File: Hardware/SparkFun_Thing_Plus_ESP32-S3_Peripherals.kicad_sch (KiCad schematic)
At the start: 27 parts, among them J2 microSD_Friction, J3 JST_2mm_LiPo, J5 Qwiic_Vertical, U1 AP2112K-3.3, U7 MCP73831, U8 MAX17048

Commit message: Update rev number
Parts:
- renumbered C15 to C12, C14 to C2, C5 to C3, C18 to C4, C19 to C5, C16 to C8, C12 to C9, JP3 to JP1, U8 to U4, U7 to U5
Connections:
- net ESP33/SDIO3: now also R6.2; no longer R1.2
- net ESP34/SDIO_CMD: now also R1.2; no longer R6.2
- net ESP38/SDIO_CLK: now also R2.2; no longer R5.2
- net ESP39/SDIO0: now also R3.2; no longer R4.2
- net ESP40/SDIO1: now also R4.2; no longer R3.2
- net ESP47/SDIO2: now also R5.2; no longer R2.2
- net GND: now also U4.9 (GND)
- net +3.3V renamed 3.3V
- net +5V renamed 5V
- new net: J3.NC1, J3.NC2
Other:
- note added: "7-bit I2C Address: 0x36"

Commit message: Updates post review
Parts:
- added LP1: ~, SparkFun-Jumper:SMT-JUMPER_3_1-NC_TRACE_SILK, symbol SparkFun-Jumper:SolderJumper_3_Bridged12
- added Q1: DMG2305UX, SparkFun-Semiconductor-Standard:SOT23-3, symbol SparkFun-DiscreteSemi:Q_PMOS_4.2A_20V
- added R17, R18: 100k, SparkFun-Resistor:R_0402_1005Metric, symbol SparkFun-Resistor:100k_0402
- C3: value 1.0uF -> 10uF; footprint SparkFun-Capacitor:C_0402_1005Metric -> SparkFun-Capacitor:C_0603_1608Metric; symbol SparkFun-Capacitor:1.0uF_0402_16V_10% -> SparkFun-Capacitor:10uF_0603_6.3V_20%; PROD_ID CAP-14969 -> CAP-11015; Tolerance 10% -> 20%; Voltage 16V -> 6.3V
- U1: value AP2112K-3.3 -> RT9080-3.3; symbol SparkFun-Regulator:AP2112K-3.3 -> SparkFun-Regulator:RT9080-3.3; Imax (none) -> 600mA; Iq (none) -> 4µA; PROD_ID VREG-12457 -> VREG-19034; VMax (none) -> 6V
- renumbered JP1 to CHG1
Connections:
- net 3.3V: now also Q1.2 (S), R18.1; no longer C4.1, C5.1, C8.1, D6.1 (VDD), J2.4 (VDD), R1.1, R2.1, R3.1, R4.1, R5.1, R6.1
- net ESP45/Q_EN: now also R17.2
- net GND: now also LP1.1 (A), R17.1
- net ESP35/~{ALRT}: now reaches U4.5 (~{ALRT})
- net 5V renamed VIN
- new net: LP1.2 (C), Q1.1 (G), R18.2
- new net 3.3V_P: C4.1, C5.1, C8.1, D6.1 (VDD), J2.4 (VDD), Q1.3 (D), R1.1, R2.1, R3.1, R4.1, R5.1, R6.1
- new net ESP41/LP_CTL: LP1.3 (B)
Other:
- note added: "Move LP jumper to 41 side to enable low power control"
- note added: "Peripheral Power Control"
- moved on the sheet: C3, U1

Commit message: Add default on to Qwiic power.
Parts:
- added R19: 100k, SparkFun-Resistor:R_0402_1005Metric, symbol SparkFun-Resistor:100k_0402
- JP2: renamed from LP1; value ~ -> LP_CTL
- R17: value 100k -> 10k; symbol SparkFun-Resistor:100k_0402 -> SparkFun-Resistor:10k_0402; PROD_ID RES-13495 -> RES-14241
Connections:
- net 3.3V_P: now also R17.1
- net ESP45/Q_EN: now also R19.1
- net GND: now also R19.2; no longer R17.1
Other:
- note added: "Default: 3.3V_P is on, Q_EN is pulled up If LP_CTL jumper is cut, 3.3V_P is off, and Q_EN is pulled down"
- note added: "Move LP jumper to LP_CTL side to enable low power control"
- note removed: "Move LP jumper to 41 side to enable low power control"
- moved on the sheet: C3, J5, R17, R3, R4, U1

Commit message: Revise layout post design review
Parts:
- removed JP2: LP_CTL, SparkFun-Jumper:SMT-JUMPER_3_1-NC_TRACE_SILK, symbol SparkFun-Jumper:SolderJumper_3_Bridged12
- removed Q1: DMG2305UX, SparkFun-Semiconductor-Standard:SOT23-3, symbol SparkFun-DiscreteSemi:Q_PMOS_4.2A_20V
- removed R18: 100k, SparkFun-Resistor:R_0402_1005Metric, symbol SparkFun-Resistor:100k_0402
- added C14: 2.2uF, SparkFun-Capacitor:C_0402_1005Metric, symbol SparkFun-Capacitor:2.2uF_0402_10V_10%
- added JP2: LP_CTL, SparkFun-Jumper:SMT-JUMPER_2_NC_TRACE_SILK, symbol SparkFun-Jumper:SolderJumper_2_Bridged
- C3: footprint SparkFun-Capacitor:C_0603_1608Metric -> SparkFun-Capacitor:C_0402_1005Metric; symbol SparkFun-Capacitor:10uF_0603_6.3V_20% -> SparkFun-Capacitor:10uF_0402_6.3V_20%; PROD_ID CAP-11015 -> CAP-14848
- JP3: renamed from CHG1; value ~ -> CHG
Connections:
- net Q3V3 is gone; now on net 3.3V_P: C3.1, J5.2 (Pin_2), R3.1, R4.1, U1.5 (VOUT)
- net 3.3V: now also JP2.2 (B)
- net 3.3V_P: now also D6.4 (VDD); no longer D6.1 (VDD), R17.1
- net ESP46/LED: now also D6.3 (DIN); no longer D6.4 (DIN)
- net GND: now also D6.2 (VSS), C14.2; no longer D6.3 (VSS)
- net VIN: now also C14.1
- net at TP1.1: now also D6.1 (DOUT); no longer D6.2 (DOUT)
- new net: JP2.1 (A), R17.1
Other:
- note added: "Default: Peripheral Power is on If LP_CTL jumper is cut and ESP32 goes to sleep, Peripheral Power is turned off."
- note removed: "Default: 3.3V_P is on, Q_EN is pulled up If LP_CTL jumper is cut, 3.3V_P is off, and Q_EN is pulled down"
- note removed: "Move LP jumper to LP_CTL side to enable low power control"
- note removed: "Qwiic"
- moved on the sheet: C3, C4, C5, J2, J5, R1, R17, R19, R2, R3, R4, R5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

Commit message: Fix 330 prod ID. Update parts to new naming conventions
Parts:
- C12: Tolerance 10% -> 20%
- J3: footprint SparkFun-Connector:JST-2-SMD -> SparkFun-Connector:JST_SMD_2.0mm-2
- J5: value Qwiic_Vertical -> Qwiic_RA; footprint SparkFun-Connector:JST04_1MM_RA -> SparkFun-Connector:JST_SMD_1.0mm-4_RA
- JP2: value LP_CTL -> ~; footprint SparkFun-Jumper:SMT-JUMPER_2_NC_TRACE_SILK -> SparkFun-Jumper:Jumper_2_NC_Trace
- JP3: value CHG -> ~; footprint SparkFun-Jumper:SMT-JUMPER_2_NC_TRACE_SILK -> SparkFun-Jumper:Jumper_2_NC_Trace
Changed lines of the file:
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@@
       (effects (font (size 1.27 1.27)) (justify right))
     )
-    (property "Value" "LP_CTL" (at 49.53 40.64 0)
-      (effects (font (size 1.27 1.27)))
-    )
-    (property "Footprint" "SparkFun-Jumper:SMT-JUMPER_2_NC_TRACE_SILK" (at 51.562 40.894 0)
+    (property "Value" "~" (at 49.53 40.64 0)
+      (effects (font (size 1.27 1.27)))
+    )
+    (property "Footprint" "SparkFun-Jumper:Jumper_2_NC_Trace" (at 51.562 40.894 0)
       (effects (font (size 1.27 1.27)) hide)
     )
@@
       (effects (font (size 1.27 1.27)) (justify left))
     )
-    (property "Tolerance" "10%" (at 257.81 110.49 0)
+    (property "Tolerance" "20%" (at 257.81 110.49 0)
       (effects (font (size 1.27 1.27)) (justify left))
     )
@@
       (effects (font (size 1.27 1.27)))
     )
-    (property "Footprint" "SparkFun-Connector:JST-2-SMD" (at 271.78 113.03 0)
+    (property "Footprint" "SparkFun-Connector:JST_SMD_2.0mm-2" (at 271.78 113.03 0)
       (effects (font (size 1.27 1.27)) hide)
     )
@@
       (effects (font (size 1.27 1.27)) (justify left))
     )
-    (property "Value" "Qwiic_Vertical" (at 85.09 110.49 0)
-      (effects (font (size 1.27 1.27)) (justify left))
-    )
-    (property "Footprint" "SparkFun-Connector:JST04_1MM_RA" (at 76.2 120.65 0)
+    (property "Value" "Qwiic_RA" (at 85.09 110.49 0)
+      (effects (font (size 1.27 1.27)) (justify left))
+    )
+    (property "Footprint" "SparkFun-Connector:JST_SMD_1.0mm-4_RA" (at 76.2 120.65 0)
       (effects (font (size 1.27 1.27)) hide)
     )
@@
       (effects (font (size 1.27 1.27)))
     )
-    (property "Value" "CHG" (at 212.09 104.14 0)
-      (effects (font (size 1.27 1.27)))
-    )
-    (property "Footprint" "SparkFun-Jumper:SMT-JUMPER_2_NC_TRACE_SILK" (at 214.122 104.394 0)
-      (effects (font (size 1.27 1.27)) hide)
-    )
+    (property "Value" "~" (at 212.09 104.14 0)
+      (effects (font (size 1.27 1.27)))
+    )
+    (property "Footprint" "SparkFun-Jumper:Jumper_2_NC_Trace" (at 214.122 104.394 0)
+      (effects (font (size 1.27 1.27)) hide)
+    )

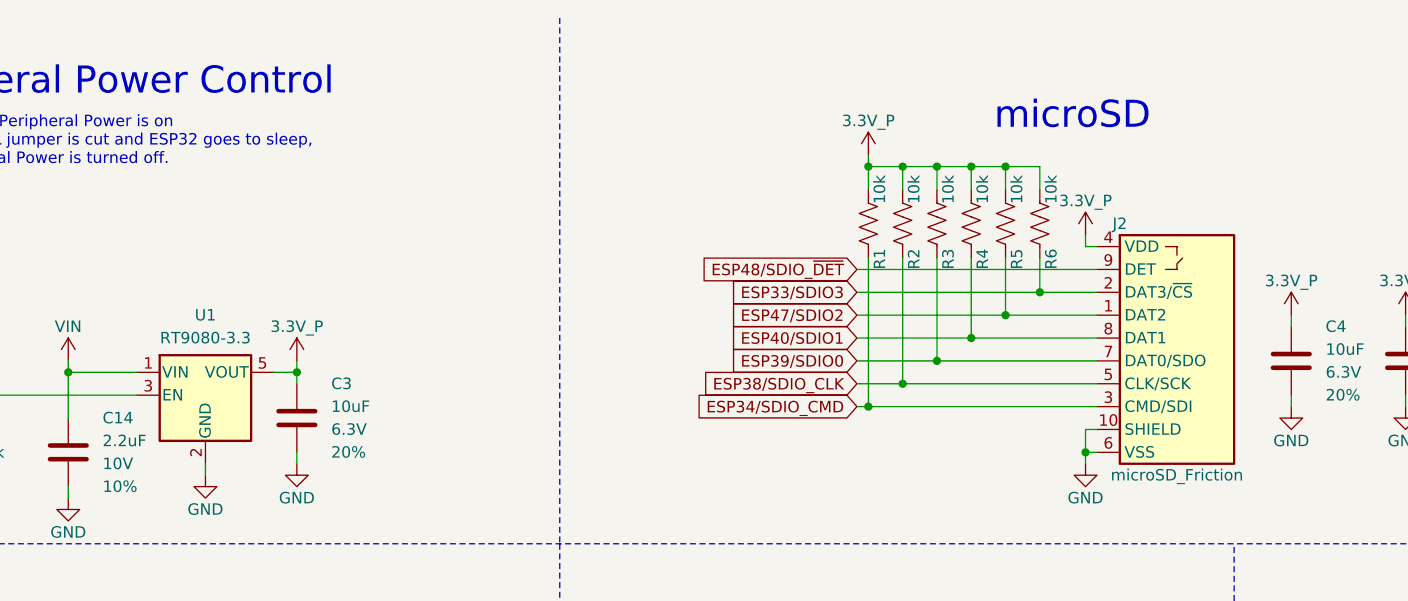
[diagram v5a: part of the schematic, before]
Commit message: Update with current models and symbols
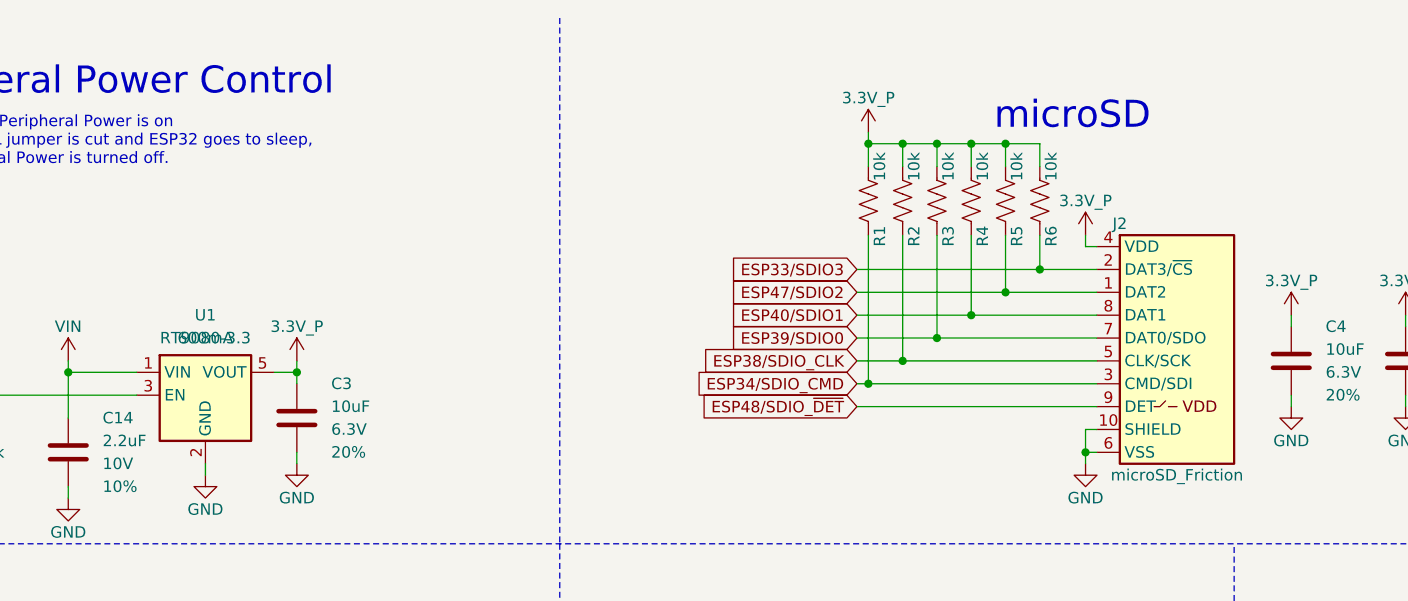
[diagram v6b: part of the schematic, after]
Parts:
- D4: footprint SparkFun-LED:LED_0603_1608Metric -> SparkFun-LED:LED_0603_1608Metric_Yellow
- D6: footprint SparkFun-LED:WS2812-2020 -> SparkFun-LED:WS2812_2020
- J2: footprint SparkFun-Connector:microSD_Friction_Fit_Atom -> SparkFun-Connector:microSD_Friction_Fit_Common
- U1: IMax (none) -> 600mA; VMax 6V -> 5.5V
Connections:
- net at J5.NC1 (NC): no longer J5.NC2 (NC)
